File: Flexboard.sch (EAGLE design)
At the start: 291 parts, among them U1 MK20DN512VLQ10

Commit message: Partially routed schematic. Pattern should duplicate for rest of board.
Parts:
- added JP1, JP10, JP2, JP3, JP4, JP5, JP6, JP7, JP8, JP9: (no value), pinhead:PINHD-1X2/90
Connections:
- new net COL_0: JP1.2, KEY_109.SW1, KEY_129.SW1, KEY_41.SW1, KEY_64.SW1, KEY_87.SW1
- new net COL_1: JP2.2, KEY_110.SW1, KEY_130.SW1, KEY_42.SW1, KEY_65.SW1, KEY_88.SW1
- new net COL_2: JP3.2, KEY_111.SW1, KEY_131.SW1, KEY_43.SW1, KEY_66.SW1, KEY_89.SW1
- new net COL_3: JP4.2, KEY_112.SW1, KEY_132.SW1, KEY_44.SW1, KEY_67.SW1, KEY_90.SW1
- new net COL_4: JP5.2, KEY_113.SW1, KEY_133.SW1, KEY_45.SW1, KEY_68.SW1, KEY_91.SW1
- new net COL_5: JP6.2, KEY_114.SW1, KEY_46.SW1, KEY_69.SW1, KEY_92.SW1
- new net COL_6: JP7.2, KEY_115.SW1, KEY_47.SW1, KEY_70.SW1, KEY_93.SW1
- new net COL_7: JP8.2, KEY_116.SW1, KEY_134.SW1, KEY_48.SW1, KEY_71.SW1, KEY_94.SW1
- new net N$1: JP2.1, KEY_2.SW1, KEY_22.SW1
- new net N$10: JP6.1, KEY_26.SW1, KEY_6.SW1
- new net N$11: D5.C, KEY_5.SW2
- new net N$12: D6.C, KEY_6.SW2
- new net N$13: D7.C, KEY_7.SW2
- new net N$14: JP7.1, KEY_27.SW1, KEY_7.SW1
- new net N$15: D8.C, KEY_8.SW2
- new net N$16: JP8.1, KEY_28.SW1, KEY_8.SW1
- new net N$17: D9.C, KEY_9.SW2
- new net N$18: D21.A, D22.A, D23.A, JP9.1
- new net N$19: D10.C, KEY_10.SW2
- new net N$2: JP1.1, KEY_1.SW1, KEY_21.SW1
- new net N$20: D31.C, KEY_31.SW2
- new net N$21: D11.C, KEY_11.SW2
- new net N$22: D40.C, KEY_40.SW2
- new net N$23: D12.C, KEY_12.SW2
- new net N$24: D39.C, KEY_39.SW2
- new net N$25: D13.C, KEY_13.SW2
- new net N$26: D25.C, KEY_25.SW2
- new net N$27: D14.C, KEY_14.SW2
- new net N$28: D38.C, KEY_38.SW2
- new net N$29: D15.C, KEY_15.SW2
- new net N$3: JP4.1, KEY_24.SW1, KEY_4.SW1
- new net N$30: D35.C, KEY_35.SW2
- new net N$31: D16.C, KEY_16.SW2
- new net N$32: D34.C, KEY_34.SW2
- new net N$33: D17.C, KEY_17.SW2
- new net N$34: D37.C, KEY_37.SW2
- new net N$35: D18.C, KEY_18.SW2
- new net N$36: D30.C, KEY_30.SW2
- new net N$37: D19.C, KEY_19.SW2
- new net N$38: D36.C, KEY_36.SW2
- new net N$39: D20.C, KEY_20.SW2
- new net N$4: JP3.1, KEY_23.SW1, KEY_3.SW1
- new net N$40: D33.C, KEY_33.SW2
- new net N$41: D23.C, KEY_23.SW2
- new net N$42: D32.C, KEY_32.SW2
- new net N$43: D29.C, KEY_29.SW2
- new net N$44: D24.C, KEY_24.SW2
- new net N$45: D28.C, KEY_28.SW2
- new net N$46: D1.A, D2.A, D3.A, JP10.1
- new net N$47: D27.C, KEY_27.SW2
- new net N$48: D22.C, KEY_22.SW2
- new net N$49: D26.C, KEY_26.SW2
- new net N$5: JP5.1, KEY_25.SW1, KEY_5.SW1
- new net N$51: D21.C, KEY_21.SW2
- new net N$6: D1.C, KEY_1.SW2
- new net N$7: D2.C, KEY_2.SW2
- new net N$8: D3.C, KEY_3.SW2
- new net N$9: D4.C, KEY_4.SW2
- new net ROW_0: D10.A, D11.A, D12.A, D13.A, D14.A, D15.A, D16.A, D17.A, D18.A, D19.A, D20.A, D4.A, D5.A, D6.A, D7.A, D8.A, D9.A, JP10.2
- new net ROW_1: D24.A, D25.A, D26.A, D27.A, D28.A, D29.A, D30.A, D31.A, D32.A, D33.A, D34.A, D35.A, D36.A, D37.A, D38.A, D39.A, D40.A, JP9.2
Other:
- moved on the sheet: D1, D10, D100, D101, D102, D103, D104, D105, D106, D107, D108, D109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

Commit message: Finished schematic wiring for PCB
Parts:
- removed JP1, JP10, JP2, JP3, JP4, JP5, JP6, JP7, JP8, JP9: (no value), pinhead:PINHD-1X2/90
- added KEY_30_OFFSET, KEY_31_OFFSET, KEY_32_OFFSET, KEY_33_OFFSET: CHERRY-MX-LED, cherrymx:CHERRY-MX-LED
- added SJ_C10, SJ_C11, SJ_C12, SJ_C13, SJ_C14, SJ_C15, SJ_C16, SJ_C17, SJ_C18, SJ_C19, SJ_C2, SJ_C3, SJ_C4, SJ_C5, SJ_C6, SJ_C7, SJ_C8, SJ_C9, SJ_R1_0, SJ_R2_0, SJ_R2_1, SJ_R3_0, SJ_R3_1, SJ_R4_0, SJ_R4_1, SJ_R5_0, SJ_R5_1, SJ_R6_0, SJ_R6_1: (no value), jumper:SJW
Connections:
- removed net N$1: JP2.1, KEY_2.SW1, KEY_22.SW1
- removed net N$2: JP1.1, KEY_1.SW1, KEY_21.SW1
- new net COL_10: KEY_119.SW1, KEY_31.SW1, KEY_31_OFFSET.SW1, KEY_51.SW1, KEY_74.SW1, KEY_97.SW1, SJ_C10.1
- new net COL_11: KEY_120.SW1, KEY_135.SW1, KEY_32.SW1, KEY_32_OFFSET.SW1, KEY_52.SW1, KEY_75.SW1, KEY_98.SW1, SJ_C11.1
- new net COL_12: KEY_121.SW1, KEY_136.SW1, KEY_33.SW1, KEY_33_OFFSET.SW1, KEY_53.SW1, KEY_76.SW1, KEY_99.SW1, SJ_C12.1
- new net COL_13: KEY_100.SW1, KEY_137.SW1, KEY_34.SW1, KEY_54.SW1, KEY_77.SW1, SJ_C13.1
- new net COL_14: KEY_35.SW1, KEY_55.SW1, KEY_78.SW1, SJ_C14.1
- new net COL_15: KEY_36.SW1, SJ_C15.1
- new net COL_16: KEY_101.SW1, KEY_122.SW1, KEY_138.SW1, KEY_37.SW1, KEY_56.SW1, KEY_79.SW1, SJ_C16.1
- new net COL_17: KEY_102.SW1, KEY_123.SW1, KEY_139.SW1, KEY_38.SW1, KEY_57.SW1, KEY_80.SW1, SJ_C17.1
- new net COL_18: KEY_103.SW1, KEY_124.SW1, KEY_140.SW1, KEY_39.SW1, KEY_58.SW1, KEY_81.SW1, SJ_C18.1
- new net COL_19: KEY_104.SW1, KEY_125.SW1, KEY_141.SW1, KEY_40.SW1, KEY_59.SW1, KEY_82.SW1, SJ_C19.1
- new net COL_20: KEY_105.SW1, KEY_126.SW1, KEY_142.SW1, KEY_60.SW1, KEY_83.SW1
- new net COL_21: KEY_106.SW1, KEY_127.SW1, KEY_143.SW1, KEY_61.SW1
- new net COL_22: KEY_107.SW1, KEY_128.SW1, KEY_144.SW1, KEY_62.SW1, KEY_85.SW1
- new net COL_23: KEY_108.SW1, KEY_145.SW1, KEY_63.SW1, KEY_86.SW1
- new net COL_8: KEY_117.SW1, KEY_29.SW1, KEY_49.SW1, KEY_72.SW1, KEY_95.SW1, SJ_C8.1
- new net COL_9: KEY_118.SW1, KEY_30.SW1, KEY_30_OFFSET.SW1, KEY_50.SW1, KEY_73.SW1, KEY_96.SW1, SJ_C9.1
- new net N$100: D68.C, KEY_68.SW2
- new net N$101: D80.C, KEY_80.SW2
- new net N$102: D69.C, KEY_69.SW2
- new net N$103: D105.A, D106.A, D107.A, D108.A, SJ_R4_1.1
- new net N$104: D70.C, KEY_70.SW2
- new net N$105: D81.C, KEY_81.SW2
- new net N$106: D71.C, KEY_71.SW2
- new net N$107: D108.C, KEY_108.SW2
- new net N$108: D72.C, KEY_72.SW2
- new net N$109: D107.C, KEY_107.SW2
- new net N$110: D73.C, KEY_73.SW2
- new net N$111: D106.C, KEY_106.SW2
- new net N$112: D74.C, KEY_74.SW2
- new net N$113: D92.C, KEY_92.SW2
- new net N$114: D75.C, KEY_75.SW2
- new net N$115: D105.C, KEY_105.SW2
- new net N$116: D76.C, KEY_76.SW2
- new net N$117: D109.C, KEY_109.SW2
- new net N$118: D77.C, KEY_77.SW2
- new net N$119: D104.C, KEY_104.SW2
- new net N$120: D78.C, KEY_78.SW2
- new net N$121: D96.C, KEY_96.SW2
- new net N$122: D103.C, KEY_103.SW2
- new net N$123: D102.C, KEY_102.SW2
- new net N$124: D126.A, D127.A, D128.A, SJ_R5_1.1
- new net N$125: D95.C, KEY_95.SW2
- new net N$126: D101.C, KEY_101.SW2
- new net N$127: D100.C, KEY_100.SW2
- new net N$128: D91.C, KEY_91.SW2
- new net N$129: D99.C, KEY_99.SW2
- new net N$130: D94.C, KEY_94.SW2
- new net N$131: D93.C, KEY_93.SW2
- new net N$132: D98.C, KEY_98.SW2
- new net N$133: D97.C, KEY_97.SW2
- new net N$134: D110.C, KEY_110.SW2
- new net N$135: D90.C, KEY_90.SW2
- new net N$136: D128.C, KEY_128.SW2
- new net N$137: D89.C, KEY_89.SW2
- new net N$138: D111.A, D112.A, D113.A, D114.A, D115.A, D116.A, D117.A, D118.A, D119.A, D120.A, D121.A, D122.A, D123.A, D124.A, D125.A, SJ_R5_0.1, SJ_R5_1.2
- new net N$139: D88.C, KEY_88.SW2
- new net N$140: D87.C, KEY_87.SW2
- new net N$141: D127.C, KEY_127.SW2
- new net N$142: D125.C, KEY_125.SW2
- new net N$143: D126.C, KEY_126.SW2
- new net N$144: D124.C, KEY_124.SW2
- new net N$145: D120.C, KEY_120.SW2
- new net N$146: D123.C, KEY_123.SW2
- new net N$147: D121.C, KEY_121.SW2
- new net N$148: D122.C, KEY_122.SW2
- new net N$149: D129.C, KEY_129.SW2
- new net N$150: D119.C, KEY_119.SW2
- new net N$151: D142.A, D143.A, D144.A, D145.A, SJ_R6_1.1
- new net N$152: D118.C, KEY_118.SW2
- new net N$153: D130.C, KEY_130.SW2
- new net N$154: D117.C, KEY_117.SW2
- new net N$155: D145.C, KEY_145.SW2
- new net N$156: D116.C, KEY_116.SW2
- new net N$157: D131.A, D132.A, D133.A, D134.A, D135.A, D136.A, D137.A, D138.A, D139.A, D140.A, D141.A, SJ_R6_0.1, SJ_R6_1.2
- new net N$158: D115.C, KEY_115.SW2
- new net N$159: D142.C, KEY_142.SW2
- new net N$160: D114.C, KEY_114.SW2
- new net N$161: D144.C, KEY_144.SW2
- new net N$162: D113.C, KEY_113.SW2
- new net N$163: D140.C, KEY_140.SW2
- new net N$164: D112.C, KEY_112.SW2
- new net N$165: D143.C, KEY_143.SW2
- new net N$166: D141.C, KEY_141.SW2
- new net N$167: D111.C, KEY_111.SW2
- new net N$168: D139.C, KEY_139.SW2
- new net N$169: D131.C, KEY_131.SW2
- new net N$171: D138.C, KEY_138.SW2
- new net N$172: D137.C, KEY_137.SW2
- new net N$174: D136.C, KEY_136.SW2
- new net N$176: D135.C, KEY_135.SW2
- new net N$178: D134.C, KEY_134.SW2
- new net N$180: D133.C, KEY_133.SW2
- new net N$183: D132.C, KEY_132.SW2
- new net N$50: KEY_11.SW1, SJ_C10.2
- new net N$52: KEY_12.SW1, SJ_C11.2
- new net N$53: KEY_13.SW1, SJ_C12.2
- new net N$54: KEY_14.SW1, SJ_C13.2
- new net N$55: KEY_15.SW1, SJ_C14.2
- new net N$56: KEY_16.SW1, SJ_C15.2
- new net N$57: KEY_17.SW1, SJ_C16.2
- new net N$58: KEY_18.SW1, SJ_C17.2
- new net N$59: KEY_19.SW1, SJ_C18.2
- new net N$60: KEY_20.SW1, SJ_C19.2
- new net N$62: D41.C, KEY_41.SW2
- new net N$63: D43.A, D44.A, D45.A, D46.A, D47.A, D48.A, D49.A, D50.A, D51.A, D52.A, D53.A, D54.A, D55.A, D56.A, D57.A, D58.A, D59.A, SJ_R2_0.1, SJ_R2_1.2
- new net N$64: D42.C, KEY_42.SW2
- new net N$65: D60.A, D61.A, D62.A, D63.A, SJ_R2_1.1
- new net N$66: D63.C, KEY_63.SW2
- new net N$67: D62.C, KEY_62.SW2
- new net N$68: D64.C, KEY_64.SW2
- new net N$69: D61.C, KEY_61.SW2
- new net N$70: D60.C, KEY_60.SW2
- new net N$71: D59.C, KEY_59.SW2
- new net N$72: D58.C, KEY_58.SW2
- new net N$73: D57.C, KEY_57.SW2
- new net N$74: D48.C, KEY_48.SW2
- new net N$75: D45.C, KEY_45.SW2
- new net N$76: D56.C, KEY_56.SW2
- new net N$77: D47.C, KEY_47.SW2
- new net N$78: D55.C, KEY_55.SW2
- new net N$79: D83.A, D84.A, D85.A, D86.A, SJ_R3_1.1
- new net N$80: D54.C, KEY_54.SW2
- new net N$81: D53.C, KEY_53.SW2
- new net N$82: D46.C, KEY_46.SW2
- new net N$83: D44.C, KEY_44.SW2
- new net N$84: D52.C, KEY_52.SW2
- new net N$85: D65.C, KEY_65.SW2
- new net N$86: D51.C, KEY_51.SW2
- new net N$87: D43.C, KEY_43.SW2
- new net N$88: D50.C, KEY_50.SW2
- new net N$89: D86.C, KEY_86.SW2
- new net N$90: D49.C, KEY_49.SW2
- new net N$91: D66.A, D67.A, D68.A, D69.A, D70.A, D71.A, D72.A, D73.A, D74.A, D75.A, D76.A, D77.A, D78.A, D79.A, D80.A, D81.A, D82.A, SJ_R3_0.1, SJ_R3_1.2
- new net N$92: D85.C, KEY_85.SW2
- new net N$93: D83.C, KEY_83.SW2
- new net N$94: D66.C, KEY_66.SW2
- new net N$95: D84.C, KEY_84.SW2
- new net N$96: D79.C, KEY_79.SW2
- new net N$97: D82.C, KEY_82.SW2
- new net N$98: D67.C, KEY_67.SW2
- new net N$99: D100.A, D101.A, D102.A, D103.A, D104.A, D89.A, D90.A, D91.A, D92.A, D93.A, D94.A, D95.A, D96.A, D97.A, D98.A, D99.A, SJ_R4_0.1, SJ_R4_1.2
- new net N67: D23.A, D24.A, D25.A, D26.A, D27.A, D28.A, D29.A, D30.A, D31.A, D32.A, D33.A, D34.A, D35.A, D36.A, D37.A, D38.A, D39.A, D40.A, SJ_R1_0.1
- new net ROW_2: D41.A, D42.A, SJ_R2_0.2
- new net ROW_3: D64.A, D65.A, SJ_R3_0.2
- new net ROW_4: D87.A, D88.A, SJ_R4_0.2
- new net ROW_5: D109.A, D110.A, SJ_R5_0.2
- new net ROW_6: D129.A, D130.A, SJ_R6_0.2
- net COL_0: now also KEY_1.SW1, KEY_21.SW1; no longer JP1.2
- net COL_1: now also KEY_2.SW1, KEY_22.SW1; no longer JP2.2
- net COL_2: now also KEY_23.SW1, SJ_C2.1; no longer JP3.2
- net COL_3: now also KEY_24.SW1, SJ_C3.1; no longer JP4.2
- net COL_4: now also KEY_25.SW1, SJ_C4.1; no longer JP5.2
- net COL_5: now also KEY_26.SW1, SJ_C5.1; no longer JP6.2
- net COL_6: now also KEY_27.SW1, SJ_C6.1; no longer JP7.2
- net COL_7: now also KEY_28.SW1, SJ_C7.1; no longer JP8.2
- net N$10: now also SJ_C5.2; no longer JP6.1, KEY_26.SW1
- net N$14: now also SJ_C6.2; no longer JP7.1, KEY_27.SW1
- net N$16: now also SJ_C7.2; no longer JP8.1, KEY_28.SW1
- net N$18: now also KEY_9.SW1, SJ_C8.2; no longer D21.A, D22.A, D23.A, JP9.1
- net N$20: now also KEY_31_OFFSET.SW2
- net N$3: now also KEY_3.SW1, SJ_C2.2; no longer JP4.1, KEY_24.SW1, KEY_4.SW1
- net N$36: now also KEY_30_OFFSET.SW2
- net N$4: now also KEY_4.SW1, SJ_C3.2; no longer JP3.1, KEY_23.SW1, KEY_3.SW1
- net N$40: now also KEY_33_OFFSET.SW2
- net N$42: now also KEY_32_OFFSET.SW2
- net N$46: now also KEY_10.SW1, SJ_C9.2; no longer D1.A, D2.A, D3.A, JP10.1
- net N$5: now also SJ_C4.2; no longer JP5.1, KEY_25.SW1
- net ROW_0: now also D1.A, D2.A, D3.A; no longer JP10.2
- net ROW_1: now also D21.A, D22.A, SJ_R1_0.2; no longer D24.A, D25.A, D26.A, D27.A, D28.A, D29.A, D30.A, D31.A, D32.A, D33.A, D34.A, D35.A, D36.A, D37.A, D38.A, D39.A, D40.A, JP9.2
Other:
- note added: "Cut Point"
- moved on the sheet: D1, D10, D100, D101, D102, D103, D104, D105, D106, D107, D108, D11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

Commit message: Switches laid out, some alignment needs fixing
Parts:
- KEY_30_OFFSET, KEY_31_OFFSET, KEY_32_OFFSET, KEY_33_OFFSET: value CHERRY-MX-LED -> CHERRY-MX-LED-NOPIN; device cherrymx:CHERRY-MX-LED -> cherrymx:CHERRY-MX-LED-NOPIN
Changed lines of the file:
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@@
 <part name="SJ_R5_1" library="jumper" library_urn="urn:adsk.eagle:library:252" deviceset="SJ" device="W" package3d_urn="urn:adsk.eagle:package:15507/1"/>
 <part name="SJ_R6_1" library="jumper" library_urn="urn:adsk.eagle:library:252" deviceset="SJ" device="W" package3d_urn="urn:adsk.eagle:package:15507/1"/>
-<part name="KEY_30_OFFSET" library="cherrymx" deviceset="CHERRY-MX-LED" device=""/>
-<part name="KEY_31_OFFSET" library="cherrymx" deviceset="CHERRY-MX-LED" device=""/>
-<part name="KEY_32_OFFSET" library="cherrymx" deviceset="CHERRY-MX-LED" device=""/>
-<part name="KEY_33_OFFSET" library="cherrymx" deviceset="CHERRY-MX-LED" device=""/>
+<part name="KEY_30_OFFSET" library="cherrymx" deviceset="CHERRY-MX-LED-NOPIN" device=""/>
+<part name="KEY_31_OFFSET" library="cherrymx" deviceset="CHERRY-MX-LED-NOPIN" device=""/>
+<part name="KEY_32_OFFSET" library="cherrymx" deviceset="CHERRY-MX-LED-NOPIN" device=""/>
+<part name="KEY_33_OFFSET" library="cherrymx" deviceset="CHERRY-MX-LED-NOPIN" device=""/>
 </parts>
 <sheets>
@@
 <wire x1="541.02" y1="-35.56" x2="541.02" y2="-43.18" width="0.1524" layer="91"/>
 <wire x1="541.02" y1="-43.18" x2="553.72" y2="-43.18" width="0.1524" layer="91"/>
-<pinref part="KEY_33_OFFSET" gate="G$1" pin="SW2"/>
 <wire x1="541.02" y1="-17.78" x2="538.48" y2="-17.78" width="0.1524" layer="91"/>
 <wire x1="538.48" y1="-17.78" x2="538.48" y2="-35.56" width="0.1524" layer="91"/>
 <wire x1="538.48" y1="-35.56" x2="541.02" y2="-35.56" width="0.1524" layer="91"/>
 <junction x="541.02" y="-35.56"/>
+<pinref part="KEY_33_OFFSET" gate="G$1" pin="SW2"/>
 </segment>
 </net>
@@
 <pinref part="D32" gate="G$1" pin="C"/>
 <wire x1="497.84" y1="-43.18" x2="510.54" y2="-43.18" width="0.1524" layer="91"/>
-<pinref part="KEY_32_OFFSET" gate="G$1" pin="SW2"/>
 <wire x1="497.84" y1="-17.78" x2="495.3" y2="-17.78" width="0.1524" layer="91"/>
 <wire x1="495.3" y1="-17.78" x2="495.3" y2="-35.56" width="0.1524" layer="91"/>
 <wire x1="495.3" y1="-35.56" x2="497.84" y2="-35.56" width="0.1524" layer="91"/>
 <junction x="497.84" y="-35.56"/>
+<pinref part="KEY_32_OFFSET" gate="G$1" pin="SW2"/>
 </segment>
 </net>
@@
 <pinref part="D31" gate="G$1" pin="C"/>
 <wire x1="457.2" y1="-43.18" x2="469.9" y2="-43.18" width="0.1524" layer="91"/>
-<pinref part="KEY_31_OFFSET" gate="G$1" pin="SW2"/>
 <wire x1="457.2" y1="-17.78" x2="454.66" y2="-17.78" width="0.1524" layer="91"/>
 <wire x1="454.66" y1="-17.78" x2="454.66" y2="-35.56" width="0.1524" layer="91"/>
 <wire x1="454.66" y1="-35.56" x2="457.2" y2="-35.56" width="0.1524" layer="91"/>
 <junction x="457.2" y="-35.56"/>
+<pinref part="KEY_31_OFFSET" gate="G$1" pin="SW2"/>
 </segment>
 </net>
@@
 <pinref part="D30" gate="G$1" pin="C"/>
 <wire x1="416.56" y1="-43.18" x2="429.26" y2="-43.18" width="0.1524" layer="91"/>
-<pinref part="KEY_30_OFFSET" gate="G$1" pin="SW2"/>
 <wire x1="416.56" y1="-17.78" x2="414.02" y2="-17.78" width="0.1524" layer="91"/>
 <wire x1="414.02" y1="-17.78" x2="414.02" y2="-35.56" width="0.1524" layer="91"/>
 <wire x1="414.02" y1="-35.56" x2="416.56" y2="-35.56" width="0.1524" layer="91"/>
 <junction x="416.56" y="-35.56"/>
+<pinref part="KEY_30_OFFSET" gate="G$1" pin="SW2"/>
 </segment>
 </net>
@@
 <wire x1="411.48" y1="-5.08" x2="411.48" y2="-12.7" width="0.1524" layer="91"/>
 <junction x="411.48" y="-68.58"/>
-<pinref part="KEY_30_OFFSET" gate="G$1" pin="SW1"/>
 <wire x1="411.48" y1="-12.7" x2="411.48" y2="-30.48" width="0.1524" layer="91"/>
 <wire x1="411.48" y1="-30.48" x2="411.48" y2="-68.58" width="0.1524" layer="91"/>
@@
 <wire x1="416.56" y1="-30.48" x2="411.48" y2="-30.48" width="0.1524" layer="91"/>
 <junction x="411.48" y="-30.48"/>
+<pinref part="KEY_30_OFFSET" gate="G$1" pin="SW1"/>
 </segment>
 </net>
@@
 <wire x1="452.12" y1="-5.08" x2="452.12" y2="-12.7" width="0.1524" layer="91"/>
 <junction x="452.12" y="-68.58"/>
-<pinref part="KEY_31_OFFSET" gate="G$1" pin="SW1"/>
 <wire x1="452.12" y1="-12.7" x2="452.12" y2="-30.48" width="0.1524" layer="91"/>
 <wire x1="452.12" y1="-30.48" x2="452.12" y2="-68.58" width="0.1524" layer="91"/>
@@
 <wire x1="457.2" y1="-30.48" x2="452.12" y2="-30.48" width="0.1524" layer="91"/>
 <junction x="452.12" y="-30.48"/>
+<pinref part="KEY_31_OFFSET" gate="G$1" pin="SW1"/>
 </segment>
 </net>
@@
 <wire x1="497.84" y1="-30.48" x2="492.76" y2="-30.48" width="0.1524" layer="91"/>
 <junction x="492.76" y="-30.48"/>
-<pinref part="KEY_32_OFFSET" gate="G$1" pin="SW1"/>
 <wire x1="497.84" y1="-12.7" x2="492.76" y2="-12.7" width="0.1524" layer="91"/>
 <junction x="492.76" y="-12.7"/>
+<pinref part="KEY_32_OFFSET" gate="G$1" pin="SW1"/>
 </segment>
 </net>
@@
 <wire x1="535.94" y1="-5.08" x2="535.94" y2="-12.7" width="0.1524" layer="91"/>
 <junction x="535.94" y="-68.58"/>
-<pinref part="KEY_33_OFFSET" gate="G$1" pin="SW1"/>
 <wire x1="535.94" y1="-12.7" x2="535.94" y2="-30.48" width="0.1524" layer="91"/>
 <wire x1="535.94" y1="-30.48" x2="535.94" y2="-68.58" width="0.1524" layer="91"/>
@@
 <wire x1="541.02" y1="-30.48" x2="535.94" y2="-30.48" width="0.1524" layer="91"/>
 <junction x="535.94" y="-30.48"/>
-</segment>
-</net>
+<pinref part="KEY_33_OFFSET" gate="G$1" pin="SW1"/>
+</segment>
+</net>

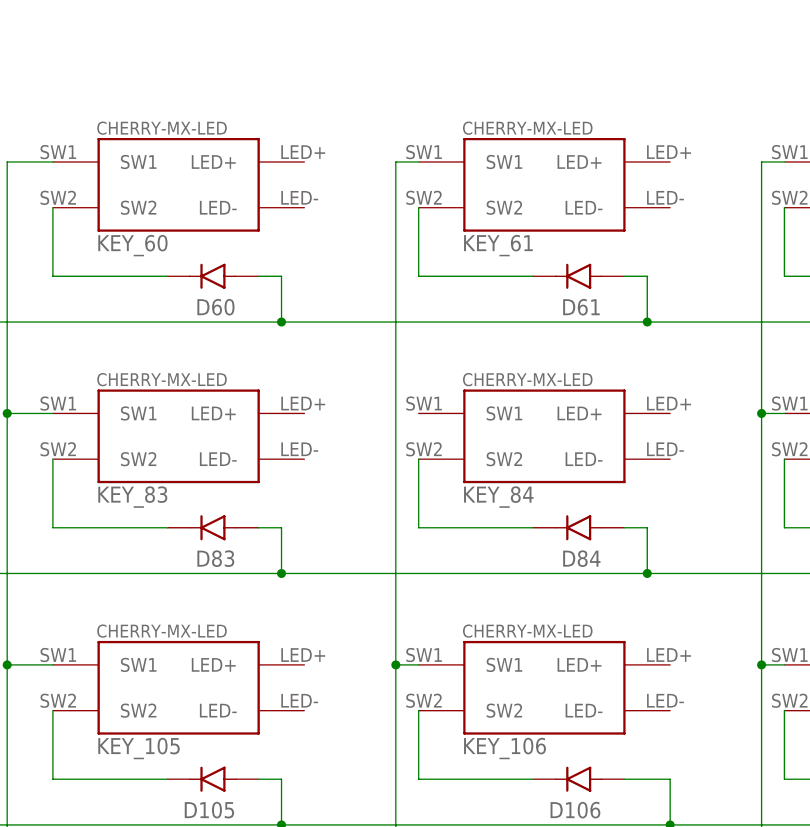
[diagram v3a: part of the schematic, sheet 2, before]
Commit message: Finished routing keyboard switches and diodes
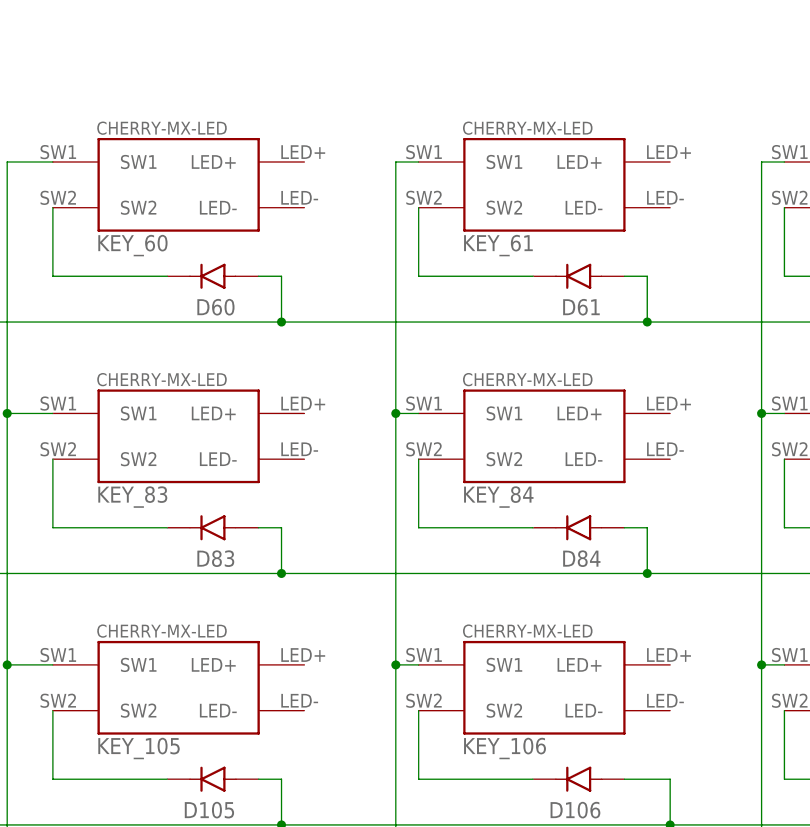
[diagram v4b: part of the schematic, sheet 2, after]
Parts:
- KEY_30, KEY_31, KEY_32, KEY_33, KEY_34: value CHERRY-MX-LED -> CHERRY-MX-LED-NOPIN; device cherrymx:CHERRY-MX-LED -> cherrymx:CHERRY-MX-LED-NOPIN
- KEY_30_OFFSET, KEY_31_OFFSET, KEY_32_OFFSET, KEY_33_OFFSET: value CHERRY-MX-LED-NOPIN -> CHERRY-MX-LED; device cherrymx:CHERRY-MX-LED-NOPIN -> cherrymx:CHERRY-MX-LED
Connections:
- net COL_21: now also KEY_84.SW1
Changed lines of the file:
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@@
 <part name="KEY_28" library="cherrymx" deviceset="CHERRY-MX-LED" device=""/>
 <part name="KEY_29" library="cherrymx" deviceset="CHERRY-MX-LED" device=""/>
-<part name="KEY_30" library="cherrymx" deviceset="CHERRY-MX-LED" device=""/>
-<part name="KEY_31" library="cherrymx" deviceset="CHERRY-MX-LED" device=""/>
-<part name="KEY_32" library="cherrymx" deviceset="CHERRY-MX-LED" device=""/>
-<part name="KEY_33" library="cherrymx" deviceset="CHERRY-MX-LED" device=""/>
-<part name="KEY_34" library="cherrymx" deviceset="CHERRY-MX-LED" device=""/>
+<part name="KEY_30" library="cherrymx" deviceset="CHERRY-MX-LED-NOPIN" device=""/>
+<part name="KEY_31" library="cherrymx" deviceset="CHERRY-MX-LED-NOPIN" device=""/>
+<part name="KEY_32" library="cherrymx" deviceset="CHERRY-MX-LED-NOPIN" device=""/>
+<part name="KEY_33" library="cherrymx" deviceset="CHERRY-MX-LED-NOPIN" device=""/>
+<part name="KEY_34" library="cherrymx" deviceset="CHERRY-MX-LED-NOPIN" device=""/>
 <part name="KEY_35" library="cherrymx" deviceset="CHERRY-MX-LED" device=""/>
 <part name="KEY_36" library="cherrymx" deviceset="CHERRY-MX-LED" device=""/>
@@
 <part name="SJ_R5_1" library="jumper" library_urn="urn:adsk.eagle:library:252" deviceset="SJ" device="W" package3d_urn="urn:adsk.eagle:package:15507/1"/>
 <part name="SJ_R6_1" library="jumper" library_urn="urn:adsk.eagle:library:252" deviceset="SJ" device="W" package3d_urn="urn:adsk.eagle:package:15507/1"/>
-<part name="KEY_30_OFFSET" library="cherrymx" deviceset="CHERRY-MX-LED-NOPIN" device=""/>
-<part name="KEY_31_OFFSET" library="cherrymx" deviceset="CHERRY-MX-LED-NOPIN" device=""/>
-<part name="KEY_32_OFFSET" library="cherrymx" deviceset="CHERRY-MX-LED-NOPIN" device=""/>
-<part name="KEY_33_OFFSET" library="cherrymx" deviceset="CHERRY-MX-LED-NOPIN" device=""/>
+<part name="KEY_30_OFFSET" library="cherrymx" deviceset="CHERRY-MX-LED" device=""/>
+<part name="KEY_31_OFFSET" library="cherrymx" deviceset="CHERRY-MX-LED" device=""/>
+<part name="KEY_32_OFFSET" library="cherrymx" deviceset="CHERRY-MX-LED" device=""/>
+<part name="KEY_33_OFFSET" library="cherrymx" deviceset="CHERRY-MX-LED" device=""/>
 </parts>
 <sheets>
@@
 <pinref part="KEY_61" gate="G$1" pin="SW1"/>
 <wire x1="962.66" y1="-68.58" x2="960.12" y2="-68.58" width="0.1524" layer="91"/>
-<wire x1="960.12" y1="-68.58" x2="960.12" y2="-124.46" width="0.1524" layer="91"/>
+<wire x1="960.12" y1="-68.58" x2="960.12" y2="-96.52" width="0.1524" layer="91"/>
 <label x="960.12" y="-203.2" size="1.778" layer="95"/>
 <pinref part="KEY_143" gate="G$1" pin="SW1"/>
+<wire x1="960.12" y1="-96.52" x2="960.12" y2="-124.46" width="0.1524" layer="91"/>
 <wire x1="960.12" y1="-124.46" x2="960.12" y2="-152.4" width="0.1524" layer="91"/>
 <wire x1="960.12" y1="-152.4" x2="960.12" y2="-177.8" width="0.1524" layer="91"/>
@@
 <wire x1="962.66" y1="-124.46" x2="960.12" y2="-124.46" width="0.1524" layer="91"/>
 <junction x="960.12" y="-124.46"/>
-</segment>
-</net>
+<pinref part="KEY_84" gate="G$1" pin="SW1"/>
+<wire x1="962.66" y1="-96.52" x2="960.12" y2="-96.52" width="0.1524" layer="91"/>
+<junction x="960.12" y="-96.52"/>
+</segment>
+</net>
